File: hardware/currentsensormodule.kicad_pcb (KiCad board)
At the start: 2 copper layers, 97.9 x 70.4 mm, 104 parts, among them J101 USART, J102 STLink, J103 Sensor1, J104 Sensor2, J105 RJ45, J106 RJ45, U101 LM324, U103 K78L15-1000R3, U104 K78L15-1000R3, U105 AMS1117-5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

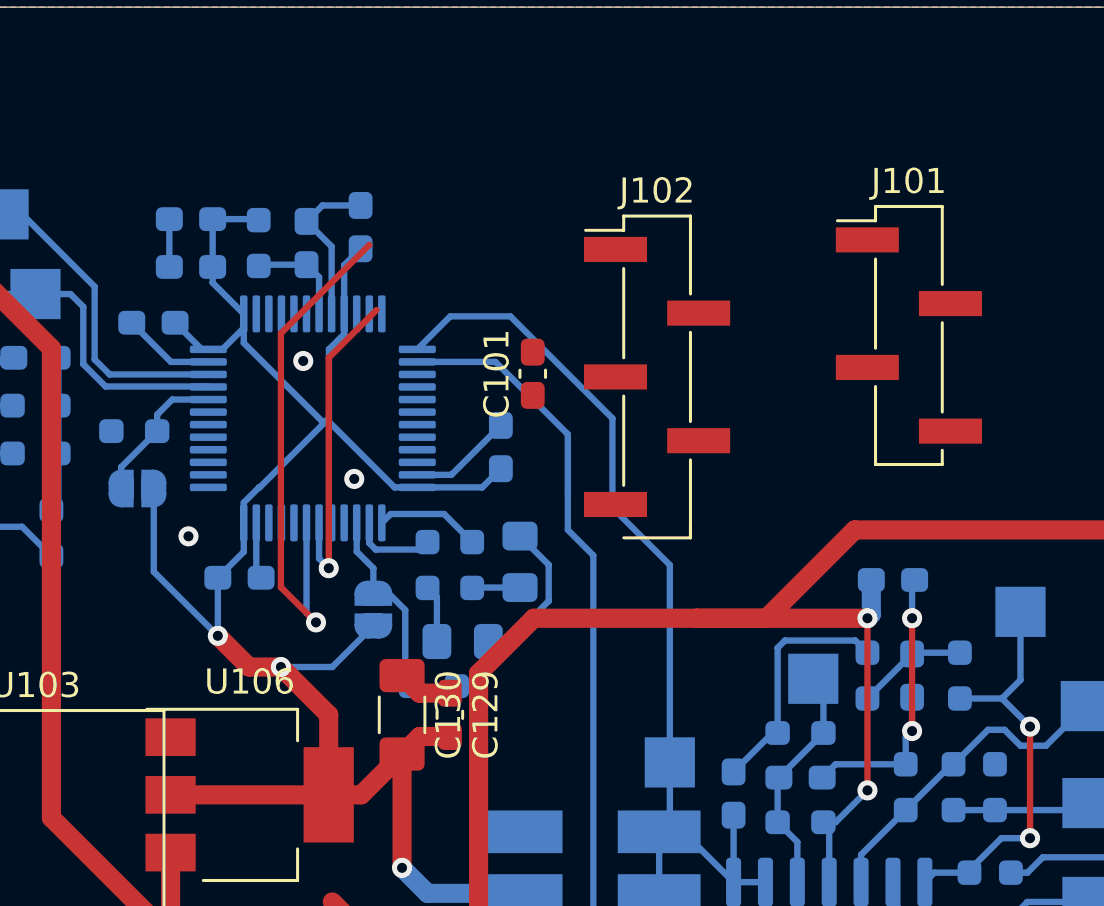
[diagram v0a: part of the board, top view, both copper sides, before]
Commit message: hardware: STM32, PCB design in progress
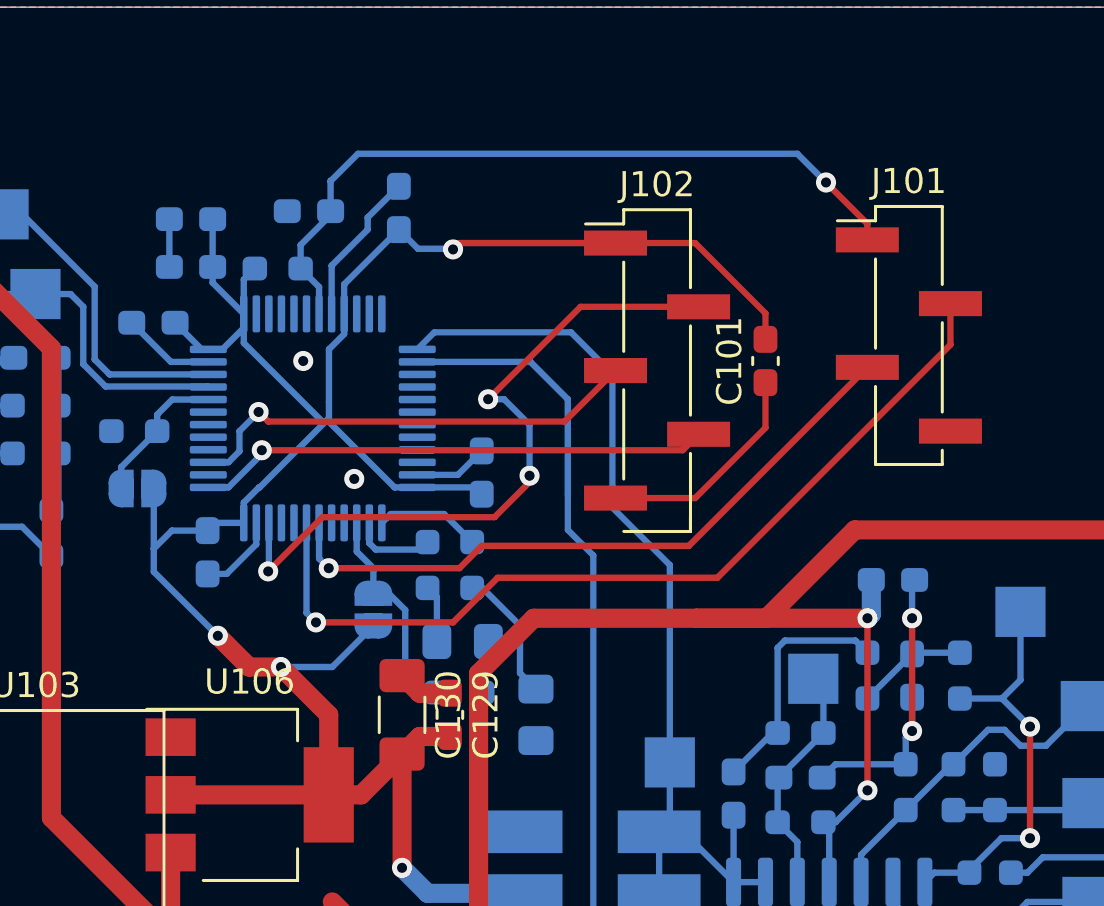
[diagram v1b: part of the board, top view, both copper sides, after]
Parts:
- moved C101 9.28 mm to (155.4, 78.2)
- moved D106 6.13 mm to (146.3, 92.3), turned to 90 degrees
- moved C115 1.70 mm to (140.8, 72.1)
- moved C113 1.63 mm to (133.2, 85.9), turned to 90 degrees
- moved C116 1.27 mm to (137.3, 72.3), turned to 0 degrees
- moved C112 1.27 mm to (144.1, 82.7)
- moved R119 1.27 mm to (136.0, 74.5), turned to 180 degrees
- moved R302 1.05 mm to (143.3, 91.4)
- moved J102 0.25 mm to (151.1, 78.6)
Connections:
- U301 pad 39: unconnected-(U301-Pad39) -> /STM32/SWO
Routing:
- net /STM32/SWDIO: track 0.00 -> 28.1 mm, vias 0 -> 3
- net /STM32/RESET: track 4.09 -> 29.8 mm, vias 0 -> 1
- net /STM32/SWCLK: track 0.00 -> 20.5 mm, vias 0 -> 1
- net /STM32/SWO: track 0.00 -> 18.5 mm, vias 0 -> 1
- net +3V3: track 89.6 -> 106.6 mm, vias 3 -> 4
- net /STM32/USART1_RX: track 21.2 -> 35.6 mm
- net /STM32/USART1_TX: track 13.0 -> 26.7 mm
- net Net-(D106-Pad2): track 1.91 -> 5.34 mm
- net GND: track 110.0 -> 112.3 mm, vias 7 -> 6
- net /STM32/JUMP0: track 7.56 -> 8.68 mm
- net /Bipolar Analog/out1: track 43.6 -> 44.5 mm
- net /Bipolar Analog/out2: track 37.9 -> 38.4 mm

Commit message: Melhoria na PCB
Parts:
- C118, C120, C123, C125, U104: moved to F.Cu
- moved C101 53.2 mm to (113.7, 111.1)
- moved J101 50.0 mm to (125.3, 112.0)
- moved J102 46.3 mm to (117.9, 110.8)
- moved C121 33.7 mm to (137.6, 84.8)
- moved C122 33.7 mm to (139.5, 84.8)
- moved C124 33.7 mm to (141.4, 84.8)
- moved C117 31.4 mm to (125.0, 80.6)
- moved C119 31.4 mm to (123.1, 80.6)
- moved D108 31.4 mm to (119.3, 82.5)
- moved F101 31.4 mm to (118.6, 78.7)
- moved C120 25.4 mm to (144.5, 109.5), turned to 180 degrees
- moved C118 25.0 mm to (144.3, 112.0), turned to 180 degrees
- moved U103 24.8 mm to (133.1, 88.8), turned to 90 degrees
- moved C115 23.4 mm to (131.7, 93.7), turned to 0 degrees
- moved U105 23.4 mm to (115.6, 98.6), turned to -90 degrees
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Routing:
- net +15V: track 142.1 -> 69.5 mm
- net -15V: track 109.5 -> 67.2 mm
- net GND: track 112.3 -> 149.2 mm
- net +5V: track 58.5 -> 24.1 mm
- net /STM32/USART1_RX: track 35.6 -> 7.73 mm
- net +3V3: track 106.6 -> 85.9 mm, vias 4 -> 1
- net /STM32/SWDIO: track 28.1 -> 11.4 mm, vias 3 -> 1
- net /STM32/USART1_TX: track 26.7 -> 12.8 mm
- net /Bipolar Analog/out1: track 44.5 -> 33.6 mm
- net /Bipolar Analog/out2: track 38.4 -> 27.8 mm
- net /POWER SUPPLY/+18V: track 19.6 -> 10.8 mm, vias 1 -> 0
- net /STM32/RESET: track 29.8 -> 21.3 mm
- net /CANBUS CONN/CAN_L: track 45.5 -> 53.1 mm
- net /Bipolar Analog/in1+: track 15.5 -> 9.28 mm
- net /STM32/SWCLK: track 20.5 -> 15.6 mm
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
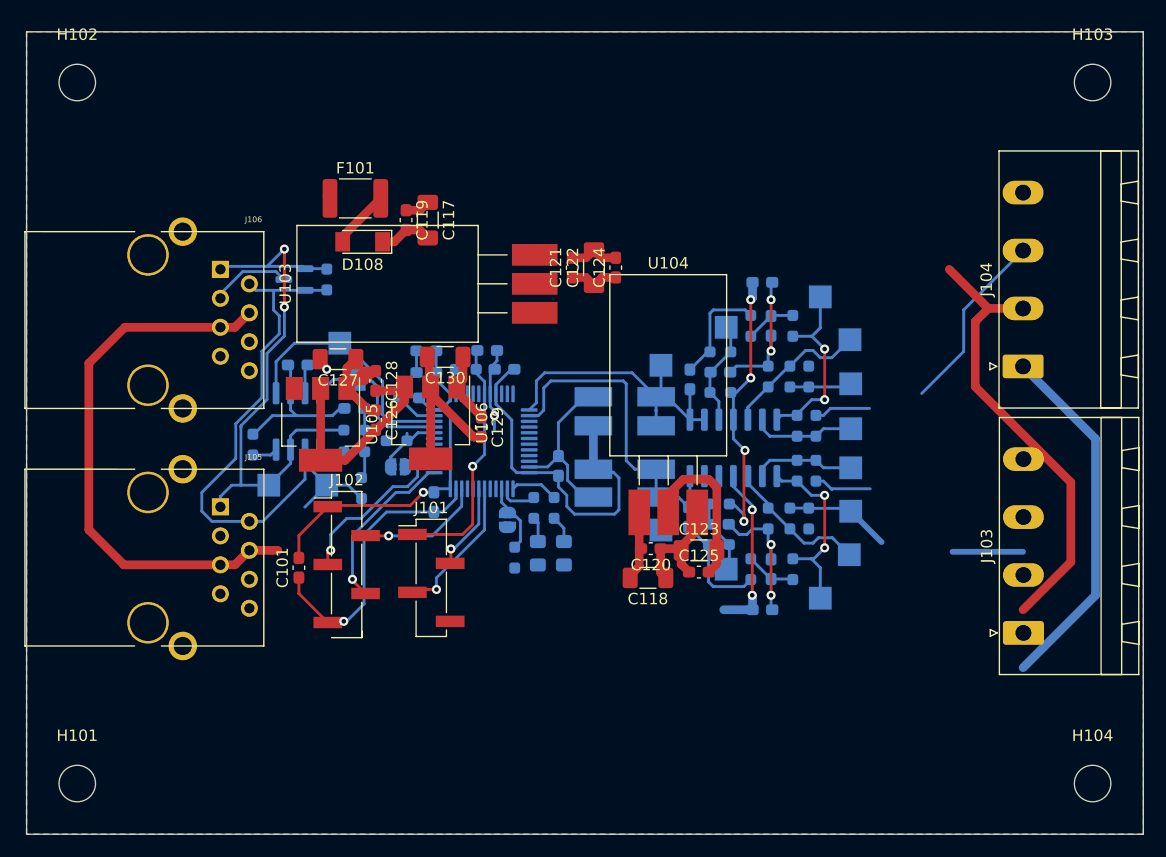
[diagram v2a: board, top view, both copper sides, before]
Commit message: PCB update: silkscreen drawn
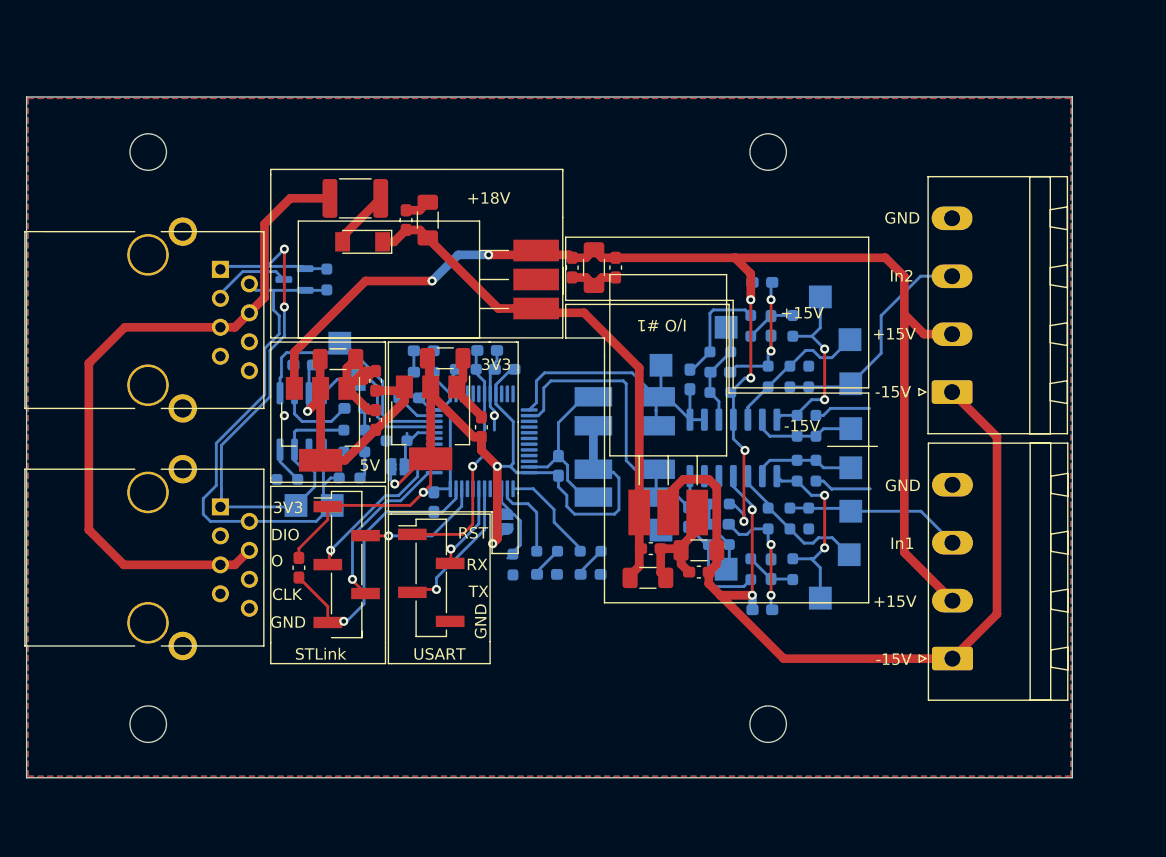
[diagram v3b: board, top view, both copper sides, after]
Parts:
- D105, D106: footprint LED_SMD:LED_0805_2012Metric_Pad1.15x1.40mm_HandSolder -> LED_SMD:LED_0603_1608Metric_Pad1.05x0.95mm_HandSolder
- moved H103 29.1 mm to (154.8, 74.7)
- moved H104 28.9 mm to (154.8, 124.8)
- moved H102 8.71 mm to (100.5, 74.7)
- moved H101 8.11 mm to (100.5, 124.8)
- moved J104 6.62 mm to (170.9, 95.7)
- moved J103 6.62 mm to (171.0, 119.1)
- moved R120 4.96 mm to (139.2, 109.7), turned to 0 degrees
- moved R124 4.29 mm to (112.6, 103.4), turned to 180 degrees
- moved R121 3.97 mm to (135.4, 109.7), turned to 0 degrees
- moved D106 2.98 mm to (139.2, 111.7), turned to 180 degrees
- moved TP503 2.97 mm to (113.4, 105.7)
- moved D105 2.02 mm to (135.4, 111.7), turned to 180 degrees
- moved TP504 1.84 mm to (116.6, 105.7)
- moved R128 1.37 mm to (118.1, 103.3), turned to 0 degrees
- moved R302 0.63 mm to (132.4, 110.8)
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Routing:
- net +15V: track 69.5 -> 126.1 mm, vias 4 -> 6
- net /POWER SUPPLY/+18V: track 10.8 -> 46.7 mm
- net +3V3: track 85.9 -> 107.5 mm, vias 1 -> 4
- net -15V: track 67.2 -> 81.3 mm
- net /CANBUS CONN/CAN_18V: track 49.2 -> 61.7 mm
- net /CANBUS CONN/CAN_H: track 49.8 -> 56.3 mm
- net /Bipolar Analog/in1+: track 9.28 -> 15.5 mm
- net +5V: track 24.1 -> 29.1 mm
- net /STM32/LED0: track 4.21 -> 9.01 mm
- net GND: track 149.2 -> 145.2 mm, vias 6 -> 7
- net /CANBUS CONN/CAN_L: track 53.1 -> 49.2 mm
- net /STM32/LED1: track 3.36 -> 7.31 mm
- net /Bipolar Analog/in2+: track 21.7 -> 20.2 mm
- net /STM32/JUMP0: track 6.67 -> 8.05 mm
- net Net-(R124-Pad1): track 2.23 -> 3.25 mm
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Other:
- board size 97.9 x 70.4 mm -> 91.7 x 59.7 mm
- board text added: "+15V"
- board text added: "+18V"
- board text added: "-15V"
- board text added: "3V3"
- board text added: "5V"
- board text added: "BOOT0"
- board text added: "CAN"
- board text added: "CLK"
- board text added: "DIO"
- board text added: "GND"
- board text added: "I/O #1"
- board text added: "I/O #2"
- board text added: "In1"
- board text added: "In2"
- board text added: "JUMP0"
- board text added: "LED0"
- board text added: "LED1"
- board text added: "O"
- board text added: "RESET"
- board text added: "RST"
- board text added: "RX"
- board text added: "STLink"
- board text added: "TX"
- board text added: "USART"

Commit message: STLink 3v3 protection diode, silkscreen updates
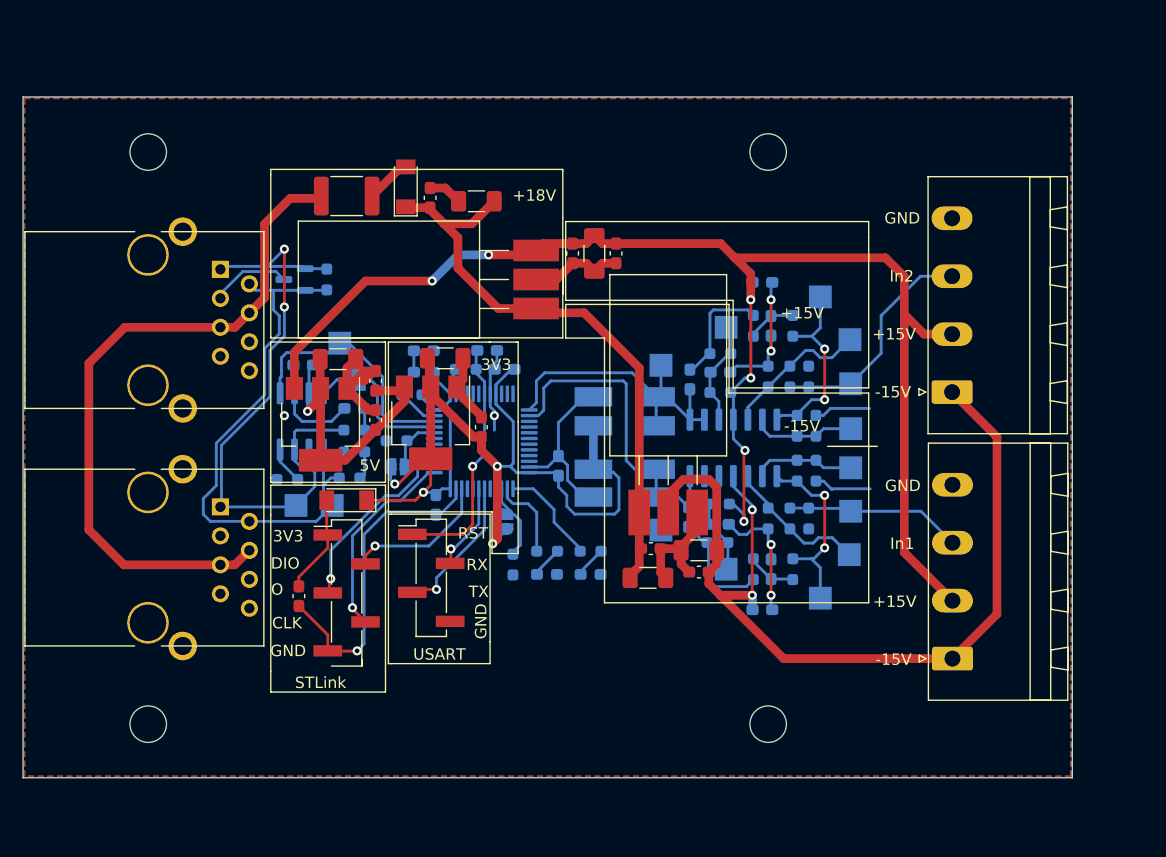
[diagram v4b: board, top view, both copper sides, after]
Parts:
- added D109: LL4148, Diode_SMD:D_MiniMELF, F.Cu at (117.9, 105.2)
- TP101: value in+ -> in+1
- TP102: value in+ -> in+2
- TP103: value op_a_in- -> op_a_in-1
- TP104: value op_a_in+ -> op_a_in+1
- TP105: value op_a_in- -> op_a_in-2
- TP106: value op_a_in+ -> op_a_in+2
- TP107: value op_a_out -> op_a_out1
- TP108: value op_a_out -> op_a_out2
- TP109: value op_b_in+ -> op_b_in+1
- TP110: value op_b_in+ -> op_b_in+2
- TP111: value op_b_out -> op_b_out1
- TP112: value op_b_out -> op_b_out2
- moved D108 6.13 mm to (123.0, 77.7), turned to 90 degrees
- moved C117 4.58 mm to (129.2, 79.0), turned to 0 degrees
- moved C119 2.88 mm to (125.2, 78.7)
- moved C101 2.49 mm to (113.7, 113.6)
- moved J102 2.49 mm to (117.9, 113.3)
- moved C121 1.24 mm to (137.7, 83.6)
- moved C122 1.24 mm to (139.6, 83.6)
- moved C124 1.24 mm to (141.5, 83.6)
- moved F101 0.79 mm to (117.9, 78.5)
- moved C114 0.40 mm to (123.6, 96.0)
- moved C113 0.30 mm to (125.7, 105.6)
- moved R113 0.23 mm to (153.5, 111.3)
- moved R114 0.23 mm to (153.5, 89.9)
- moved R115 0.22 mm to (150.4, 108.9)
- moved R116 0.15 mm to (150.6, 92.4)
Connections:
- C101 pad 2: +3V3 -> Net-(C101-Pad2)
- J102 pad 1: +3V3 -> Net-(C101-Pad2)
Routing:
- net +3V3: track 107.5 -> 98.0 mm
- net Net-(C101-Pad2): track 0.00 -> 8.63 mm
- net GND: track 145.2 -> 150.7 mm
- net /POWER SUPPLY/+18V: track 46.7 -> 52.0 mm
- net /STM32/SWO: track 14.1 -> 16.6 mm
- net /STM32/SWCLK: track 15.6 -> 18.0 mm
- net /STM32/SWDIO: track 11.4 -> 12.9 mm
- net Net-(D108-Pad2): track 5.19 -> 4.02 mm
- net /STM32/JUMP0: track 8.05 -> 7.00 mm
- net /CANBUS CONN/CAN_18V: track 61.7 -> 60.7 mm
- net /STM32/BOOT0: track 5.91 -> 5.25 mm
- net /CANBUS/CAN_TX: track 21.3 -> 21.9 mm
- net +15V: track 126.1 -> 126.6 mm
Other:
- board size 91.7 x 59.7 mm -> 92 x 59.7 mm

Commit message: hardware: analog stage adjusted for application
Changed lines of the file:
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@@
   )
   (footprint "LED_SMD:LED_0603_1608Metric_Pad1.05x0.95mm_HandSolder" (layer "B.Cu")
-    (at 135.4214 111.7092 180)
+    (at 135.421395 111.7092 180)
     (descr "LED SMD 0603 (1608 Metric), square (rectangular) end terminal, IPC_7351 nominal, (Body size source: http://www.tortai-tech.com/upload/download/2011102023233369053.pdf), generated with kicad-footprint-generator")
     (tags "LED handsolder")
@@
   (gr_line (start 106.2736 82.296) (end 105.7656 82.296) (layer "B.SilkS") (width 0.12))
   (gr_line (start 130.0988 92.8624) (end 133.1976 92.8624) (layer "B.SilkS") (width 0.12))
-  (gr_line (start 140.462 90.9828) (end 140.462 92.6084) (layer "F.SilkS") (width 0.12))
   (gr_line (start 121.2596 91.3384) (end 121.158 91.3384) (layer "F.SilkS") (width 0.12))
   (gr_line (start 132.8928 91.3384) (end 132.7404 91.3384) (layer "F.SilkS") (width 0.12))
+  (gr_line (start 137.0584 90.9828) (end 137.0584 94.488) (layer "F.SilkS") (width 0.12))
   (gr_line (start 121.2596 122.0216) (end 111.2012 122.0216) (layer "F.SilkS") (width 0.12))
   (gr_line (start 121.2596 120.1928) (end 121.2596 106.4768) (layer "F.SilkS") (width 0.12))
@@
   (gr_line (start 137.0584 87.6808) (end 151.7396 87.6808) (layer "F.SilkS") (width 0.12))
   (gr_line (start 111.2012 90.8812) (end 111.2012 90.972) (layer "F.SilkS") (width 0.12))
-  (gr_line (start 140.462 113.4364) (end 140.462 92.6084) (layer "F.SilkS") (width 0.12))
+  (gr_line (start 140.462 114.1984) (end 138.811 114.1984) (layer "F.SilkS") (width 0.12))
   (gr_line (start 136.8044 80.4164) (end 136.8044 76.3524) (layer "F.SilkS") (width 0.12))
-  (gr_line (start 137.0584 90.9828) (end 140.462 90.9828) (layer "F.SilkS") (width 0.12))
   (gr_line (start 121.793 106.426) (end 130.429 106.426) (layer "F.SilkS") (width 0.12))
   (gr_line (start 111.2012 103.632) (end 121.2596 103.632) (layer "F.SilkS") (width 0.12))
-  (gr_line (start 140.462 113.4364) (end 140.462 114.1984) (layer "F.SilkS") (width 0.12))
   (gr_line (start 121.5136 106.426) (end 121.5136 119.5324) (layer "F.SilkS") (width 0.12))
   (gr_line (start 111.2012 90.8812) (end 111.2012 76.6572) (layer "F.SilkS") (width 0.12))
@@
   (gr_line (start 126.238 76.2) (end 136.8044 76.2) (layer "F.SilkS") (width 0.12))
   (gr_line (start 121.2596 120.1928) (end 121.2596 122.0216) (layer "F.SilkS") (width 0.12))
+  (gr_line (start 137.0584 94.488) (end 138.811 94.488) (layer "F.SilkS") (width 0.12))
   (gr_line (start 126.238 76.2) (end 111.2012 76.2) (layer "F.SilkS") (width 0.12))
   (gr_line (start 136.8044 90.972) (end 136.8044 80.4164) (layer "F.SilkS") (width 0.12))
@@
   (gr_line (start 130.429 117.602) (end 130.429 119.5324) (layer "F.SilkS") (width 0.12))
   (gr_line (start 111.2012 106.4768) (end 111.2012 120.1928) (layer "F.SilkS") (width 0.12))
+  (gr_line (start 138.811 114.1984) (end 138.811 94.488) (layer "F.SilkS") (width 0.12))
   (gr_line (start 111.2012 122.0216) (end 111.2012 120.1928) (layer "F.SilkS") (width 0.12))
   (gr_line (start 121.5136 92.202) (end 121.5136 103.2764) (layer "F.SilkS") (width 0.12))
